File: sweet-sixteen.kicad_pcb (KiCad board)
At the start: 2 copper layers, 100 x 104.5 mm, 83 parts, among them P1 SDA_I, P10 VIN_O, P11 GND_O, P12 SDA_O, P13 CLK_O, P14 LE_O, P15 ~OE_O, P2 CLK_I, P3 LE_I, P4 ~OE_I, P5 CONN_02X20, P6 5V_I, P7 VIN_I, P8 GND_I, P9 5V_O, U1 STP16CPC26, U2 STP16CPC26, U20 OKI-T/3-W40, U21 OKI-T/3-W40, U3 STP16CPC26, U30 74HCT08, U31 74HCT08, U4 STP16CPC26, U5 STP16CPC26, U6 STP16CPC26, U7 STP16CPC26, U8 STP16CPC26, U9 STP16CPC26

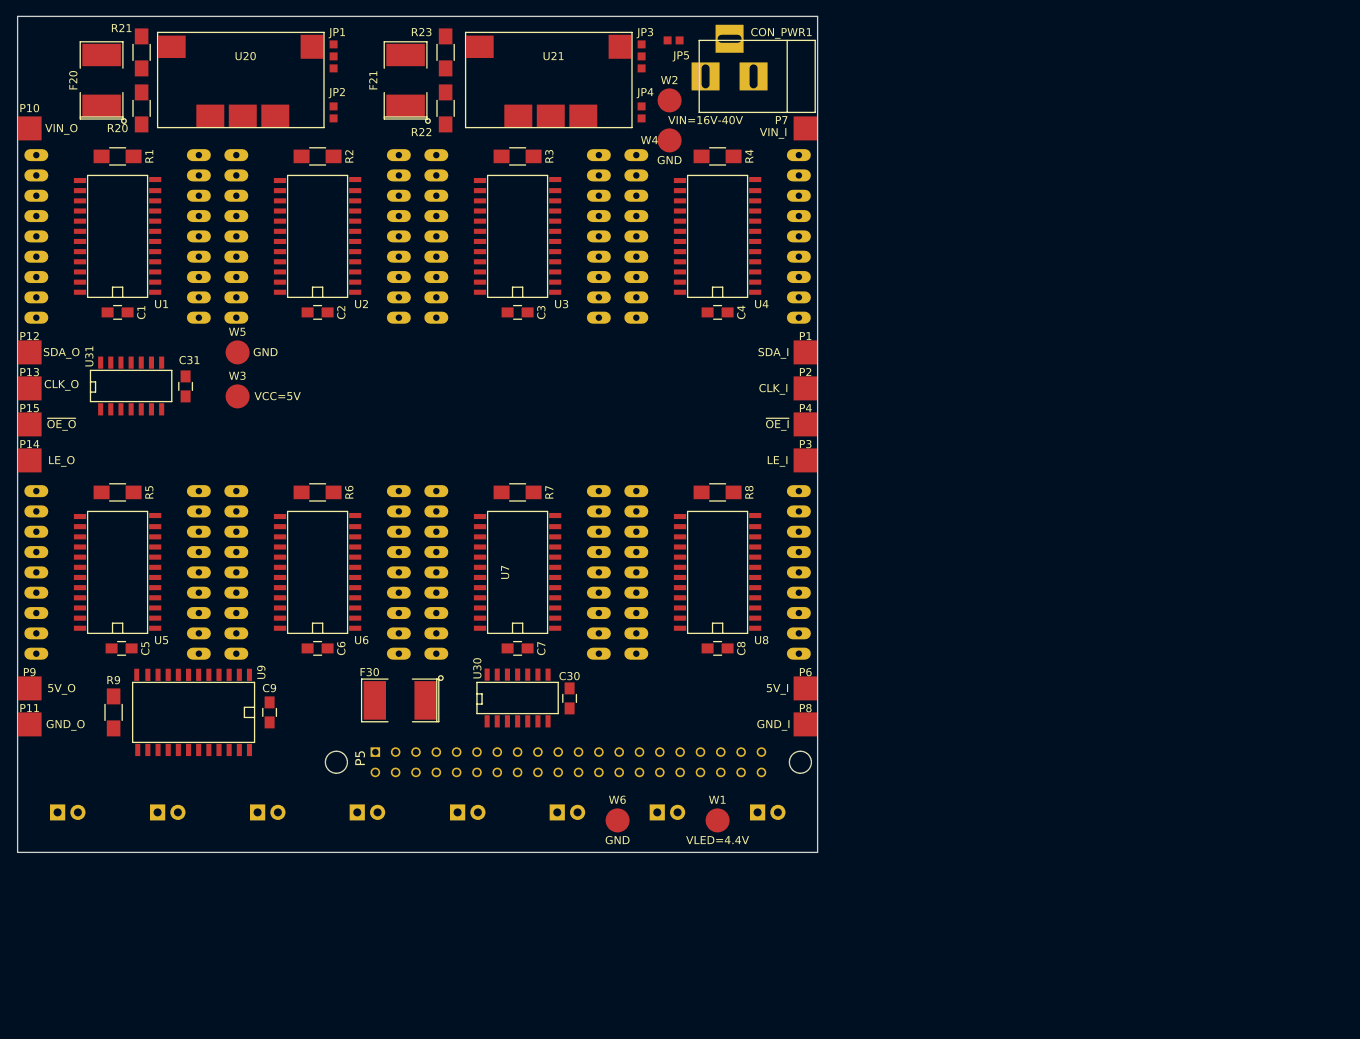
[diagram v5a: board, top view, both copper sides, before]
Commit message: move footprints to inch locations, fix outline, lock footprints
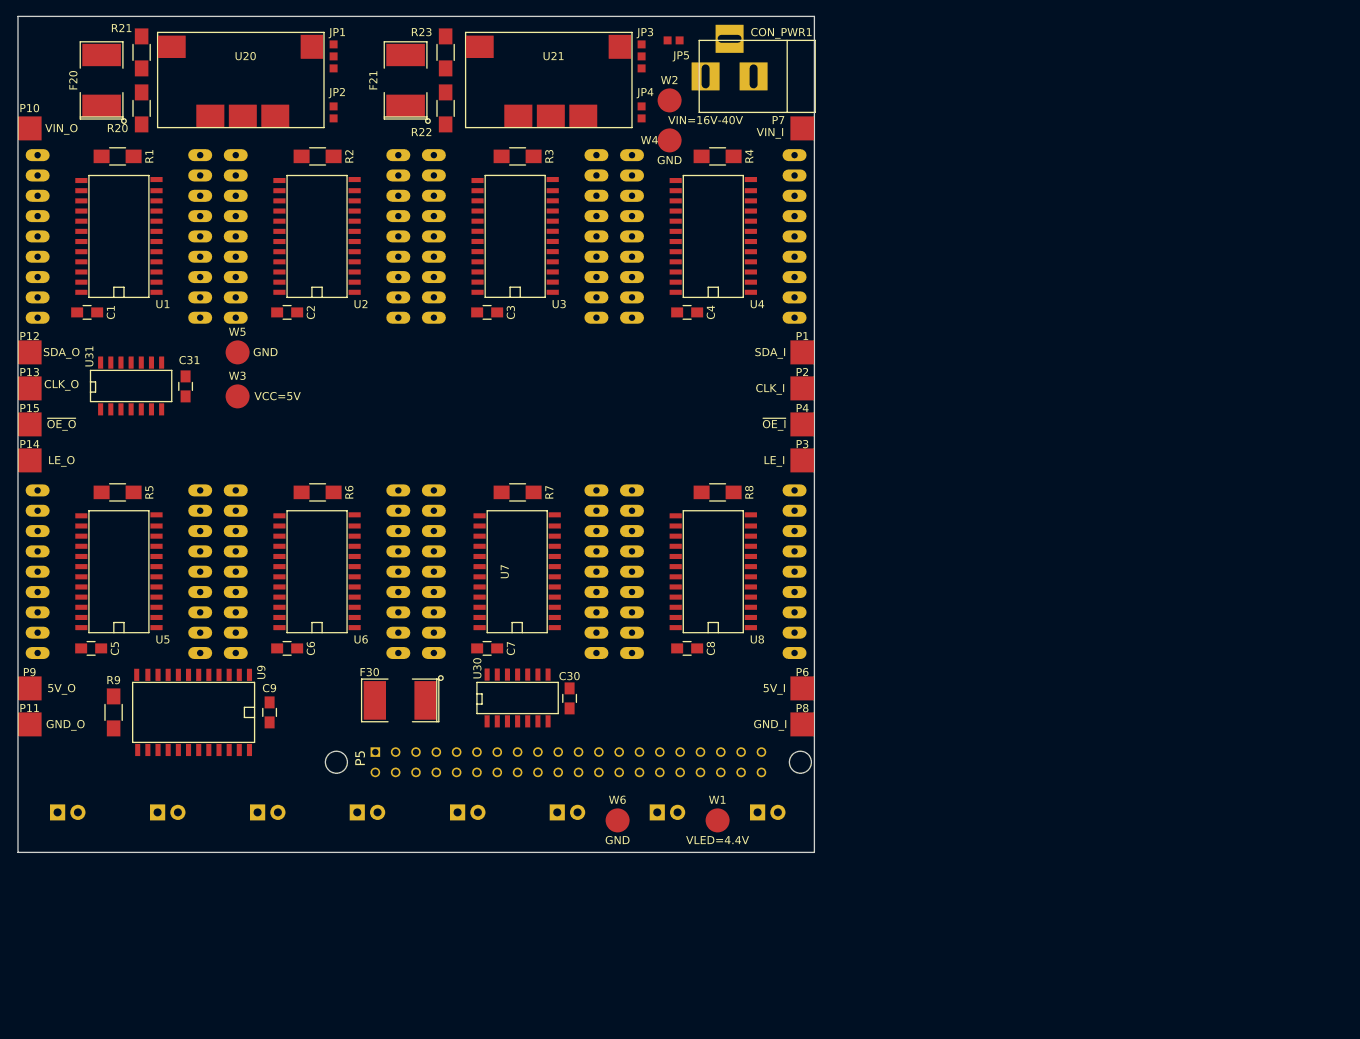
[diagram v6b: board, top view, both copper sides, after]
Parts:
- moved C1 3.81 mm to (46.2, 49.5)
- moved C2 3.81 mm to (71.2, 49.5)
- moved C3 3.81 mm to (96.2, 49.5)
- moved C4 3.81 mm to (121.2, 49.5)
- moved C5 3.81 mm to (46.7, 91.5)
- moved C6 3.81 mm to (71.2, 91.5)
- moved C7 3.81 mm to (96.2, 91.5)
- moved C8 3.81 mm to (121.2, 91.5)
- moved AFF8 0.55 mm to (124.5, 81.9)
- moved U8 0.55 mm to (124.5, 81.9)
- moved AFF4 0.54 mm to (124.5, 40.0)
- moved U4 0.54 mm to (124.5, 40.0)
- moved P1 0.40 mm to (135.6, 54.5)
- moved P2 0.40 mm to (135.6, 59.0)
- moved P3 0.40 mm to (135.6, 68.0)
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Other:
- board size 100 x 104.5 mm -> 99.5 x 104.5 mm

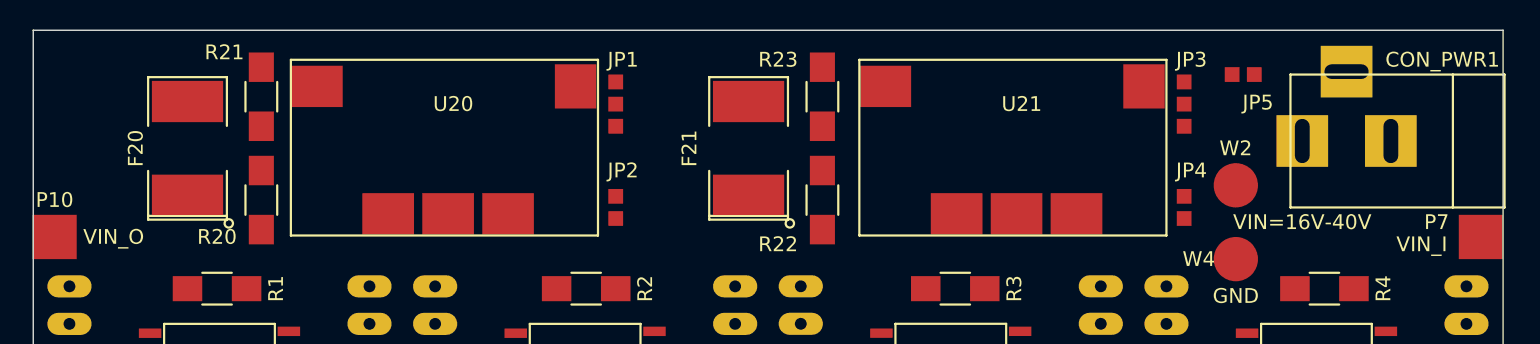
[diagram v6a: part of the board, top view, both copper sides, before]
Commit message: power tracks and via stitching
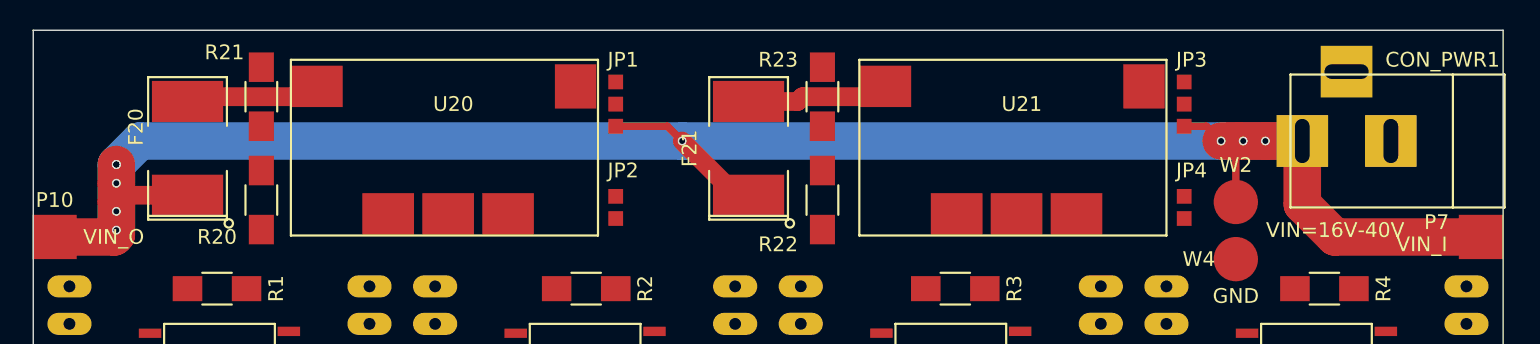
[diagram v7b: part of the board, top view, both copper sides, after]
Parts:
- removed JP5: JUMPER, jumper:SMD_Jumper_2
- moved W2 1.13 mm to (119.0, 24.1)
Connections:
- net Net-(U1-Pad22) renamed /SDA_12
- net Net-(U2-Pad22) renamed /SD23
- net Net-(U3-Pad22) renamed /SDA_34
- net Net-(U31-Pad1) renamed /SDA_O
- net Net-(U4-Pad22) renamed /SDA_45
- net Net-(U5-Pad22) renamed /SDA_56
- net Net-(U6-Pad22) renamed /SDA_67
- net Net-(U7-Pad22) renamed /SDA_78
- net Net-(U8-Pad22) renamed /SDA_89
- CON_PWR1 pad 1: Net-(CON_PWR1-Pad1) -> VIN
- P1 pad 1: /SDA -> /SDA_I
- U1 pad 2: /SDA -> /SDA_I
- U30 pad 8: /SDA -> (no net)
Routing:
- net VIN: track 0.00 -> 140.6 mm, vias 0 -> 9
- net Net-(F21-Pad2): track 0.00 -> 9.68 mm
- net Net-(F20-Pad2): track 0.00 -> 9.18 mm

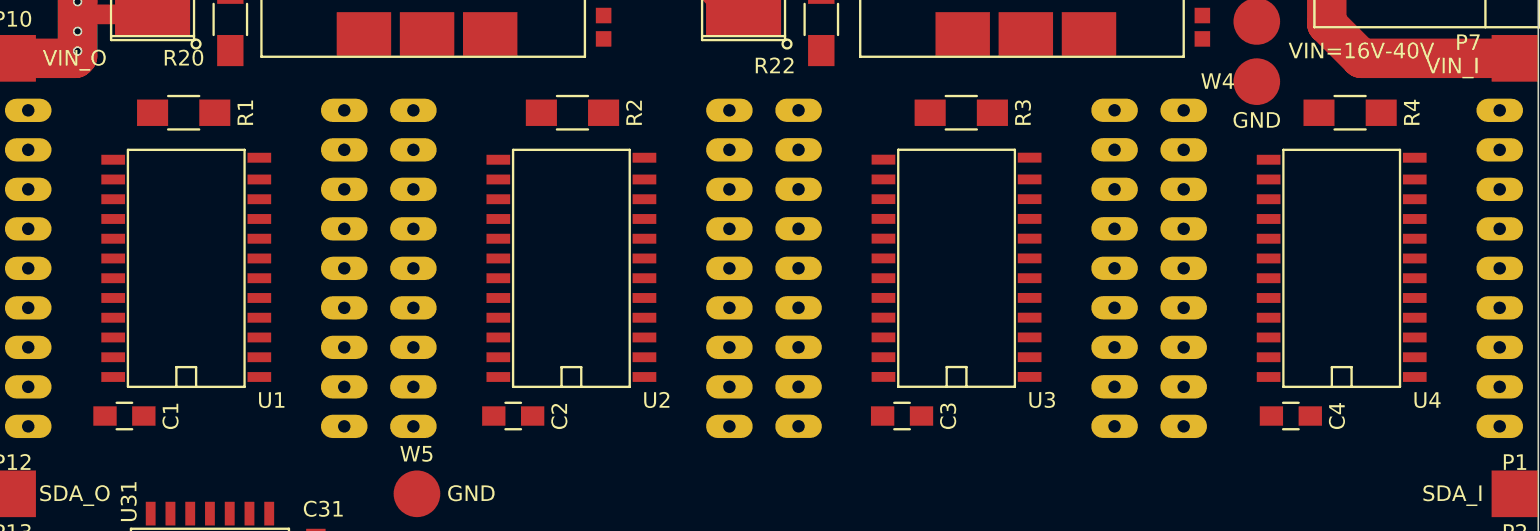
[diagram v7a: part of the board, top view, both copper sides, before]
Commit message: flip display 1-4 for bwtter routability
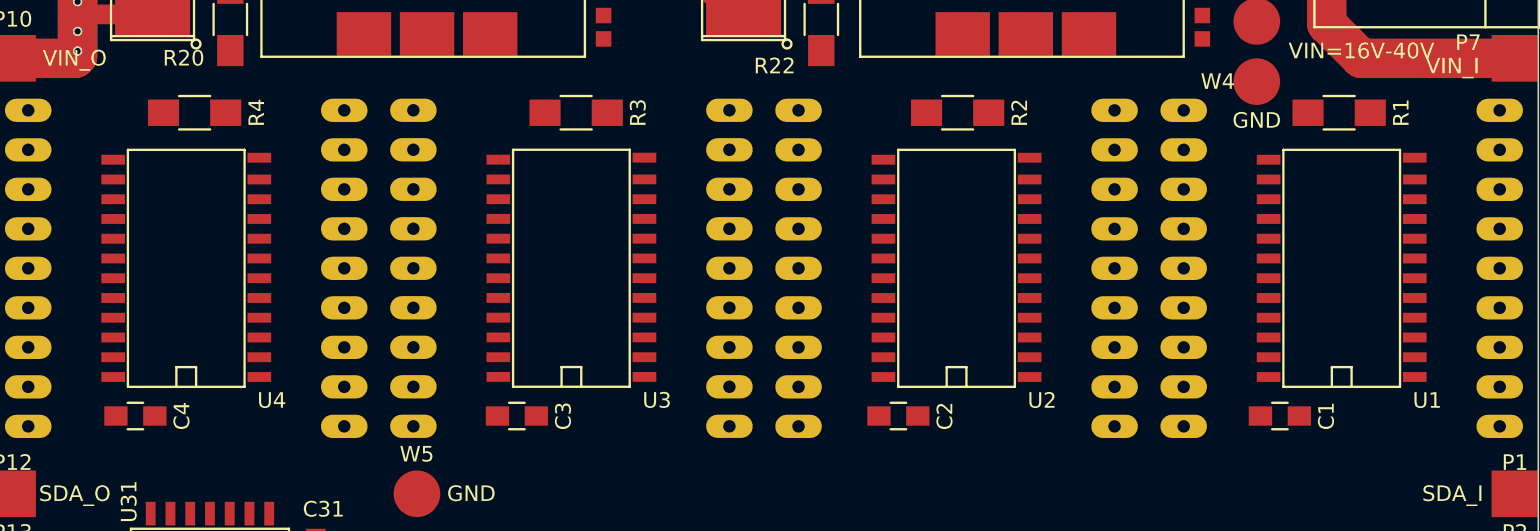
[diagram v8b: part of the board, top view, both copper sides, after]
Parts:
- moved C1 74.3 mm to (120.5, 49.5)
- moved R1 74.3 mm to (124.3, 30.0)
- moved R4 74.3 mm to (50.7, 30.0)
- moved AFF1 74.3 mm to (124.5, 40.0)
- moved AFF4 74.3 mm to (50.2, 40.0)
- moved C4 74.3 mm to (46.9, 49.5)
- moved U1 74.3 mm to (124.5, 40.0)
- moved U4 74.3 mm to (50.2, 40.0)
- moved C2 24.8 mm to (96.0, 49.5)
- moved C3 24.8 mm to (71.4, 49.5)
- moved R2 24.8 mm to (99.8, 30.0)
- moved R3 24.8 mm to (75.2, 30.0)
- moved AFF2 24.8 mm to (99.7, 40.0)
- moved AFF3 24.8 mm to (74.9, 40.0)
- moved U2 24.8 mm to (99.7, 40.0)
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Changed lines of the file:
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@@
   (general
     (links 326)
-    (no_connects 325)
+    (no_connects 317)
     (area 37.499999 12.449999 137.150001 117.050001)
     (thickness 1.6)
@@
   )
   (setup
-    (last_trace_width 1.27)
+    (last_trace_width 0.254)
     (user_trace_width 0.254)
     (user_trace_width 0.508)
@@
   )
   (module 16segments:PSA12-11 locked (layer B.Cu)
-    (at 50.165 40.005 270)
+    (at 124.46 40.005 270)
     (fp_text reference AFF1 (at -17.5 0 540) (layer B.SilkS)
       (effects (font (size 1.2 1.2) (thickness 0.15)) (justify mirror))
@@
   )
   (module 16segments:PSA12-11 locked (layer B.Cu)
-    (at 74.93 40.005 270)
+    (at 99.695 40.005 270)
     (fp_text reference AFF2 (at -17.5 0 540) (layer B.SilkS)
       (effects (font (size 1.2 1.2) (thickness 0.15)) (justify mirror))
@@
   )
   (module 16segments:PSA12-11 locked (layer B.Cu)
-    (at 99.695 40 270)
+    (at 74.93 40 270)
     (fp_text reference AFF3 (at -17.5 0 540) (layer B.SilkS)
       (effects (font (size 1.2 1.2) (thickness 0.15)) (justify mirror))
@@
   )
   (module 16segments:PSA12-11 locked (layer B.Cu)
-    (at 124.46 40.005 270)
+    (at 50.165 40.005 270)
     (fp_text reference AFF4 (at -17.5 0 540) (layer B.SilkS)
       (effects (font (size 1.2 1.2) (thickness 0.15)) (justify mirror))
@@
   )
   (module Capacitors_SMD:C_0805_HandSoldering (layer F.Cu)
-    (at 46.19 49.5)
+    (at 120.485 49.5)
     (descr "Capacitor SMD 0805, hand soldering")
     (tags "capacitor 0805")
@@
   )
   (module Capacitors_SMD:C_0805_HandSoldering (layer F.Cu)
-    (at 71.19 49.5)
+    (at 95.955 49.5)
     (descr "Capacitor SMD 0805, hand soldering")
     (tags "capacitor 0805")
@@
   )
   (module Capacitors_SMD:C_0805_HandSoldering (layer F.Cu)
-    (at 96.19 49.5)
+    (at 71.425 49.5)
     (descr "Capacitor SMD 0805, hand soldering")
     (tags "capacitor 0805")
@@
   )
   (module Capacitors_SMD:C_0805_HandSoldering (layer F.Cu)
-    (at 121.19 49.5)
+    (at 46.895 49.5)
     (descr "Capacitor SMD 0805, hand soldering")
     (tags "capacitor 0805")
@@
   )
   (module Resistors_SMD:R_1206_HandSoldering (layer F.Cu)
-    (at 50 30 180)
+    (at 124.295 30 180)
     (descr "Resistor SMD 1206, hand soldering")
     (tags "resistor 1206")
@@
   )
   (module Resistors_SMD:R_1206_HandSoldering (layer F.Cu)
-    (at 75 30 180)
+    (at 99.765 30 180)
     (descr "Resistor SMD 1206, hand soldering")
     (tags "resistor 1206")
@@
   )
   (module Resistors_SMD:R_1206_HandSoldering (layer F.Cu)
-    (at 100 30 180)
+    (at 75.235 30 180)
     (descr "Resistor SMD 1206, hand soldering")
     (tags "resistor 1206")
@@
   )
   (module Resistors_SMD:R_1206_HandSoldering (layer F.Cu)
-    (at 125 30 180)
+    (at 50.705 30 180)
     (descr "Resistor SMD 1206, hand soldering")
     (tags "resistor 1206")
@@
   )
   (module chips:STP16CPC26MTR locked (layer F.Cu)
-    (at 50.165 40.005 90)
+    (at 124.46 40.005 90)
     (attr smd)
     (fp_text reference U1 (at -8.5 5.5 180) (layer F.SilkS)
@@
   )
   (module chips:STP16CPC26MTR locked (layer F.Cu)
-    (at 74.93 40.005 90)
+    (at 99.695 40.005 90)
     (attr smd)
     (fp_text reference U2 (at -8.5 5.5 180) (layer F.SilkS)
@@
   )
   (module chips:STP16CPC26MTR locked (layer F.Cu)
-    (at 99.695 40 90)
+    (at 74.93 40 90)
     (attr smd)
     (fp_text reference U3 (at -8.5 5.5 180) (layer F.SilkS)
@@
   )
   (module chips:STP16CPC26MTR locked (layer F.Cu)
-    (at 124.46 40.005 90)
+    (at 50.165 40.005 90)
     (attr smd)
     (fp_text reference U4 (at -8.5 5.5 180) (layer F.SilkS)
